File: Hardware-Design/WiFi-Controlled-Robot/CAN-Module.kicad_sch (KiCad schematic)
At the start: 1 part

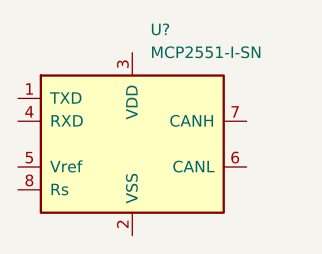
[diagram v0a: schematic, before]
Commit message: Changed CAN tranceiver to MCP2561
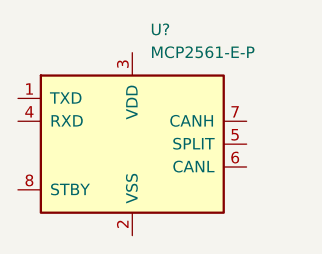
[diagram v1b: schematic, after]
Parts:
- removed U?: MCP2551-I-SN, Package_SO:SOIC-8_3.9x4.9mm_P1.27mm, symbol Interface_CAN_LIN:MCP2551-I-SN
- added U?: MCP2561-E-P, Package_DIP:DIP-8_W7.62mm, symbol Interface_CAN_LIN:MCP2561-E-P
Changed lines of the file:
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@@
     (rev "1.0.0")
   )
-  (symbol (lib_id "Interface_CAN_LIN:MCP2551-I-SN") (at 149.86 96.52 0) (unit 1)
+  (symbol (lib_id "Interface_CAN_LIN:MCP2561-E-P") (at 149.86 96.52 0) (unit 1)
     (in_bom yes) (on_board yes) (fields_autoplaced)
     (property "Reference" "U?" (id 0) (at 151.8794 83.82 0)
       (effects (font (size 1.27 1.27)) (justify left))
     )
-    (property "Value" "MCP2551-I-SN" (id 1) (at 151.8794 86.36 0)
+    (property "Value" "MCP2561-E-P" (id 1) (at 151.8794 86.36 0)
       (effects (font (size 1.27 1.27)) (justify left))
     )
-    (property "Footprint" "Package_SO:SOIC-8_3.9x4.9mm_P1.27mm" (id 2) (at 149.86 109.22 0)
+    (property "Footprint" "Package_DIP:DIP-8_W7.62mm" (id 2) (at 149.86 109.22 0)
       (effects (font (size 1.27 1.27) italic) hide)
     )
-    (property "Datasheet" "http://ww1.microchip.com/downloads/en/devicedoc/21667d.pdf" (id 3) (at 149.86 96.52 0)
+    (property "Datasheet" "http://ww1.microchip.com/downloads/en/DeviceDoc/25167A.pdf" (id 3) (at 149.86 96.52 0)
       (effects (font (size 1.27 1.27)) hide)
     )
